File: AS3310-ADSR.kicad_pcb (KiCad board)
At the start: 2 copper layers, 58 parts, among them J1 TRIGGER_IN, J2 EURO_PWR_2x5, J3 ENVELOPE_OUT, J4 GATE_IN, Q1 BC558, Q2 BC548, SW2 SW_Push, U1 LM358, U2 AS3310, U3 LM358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

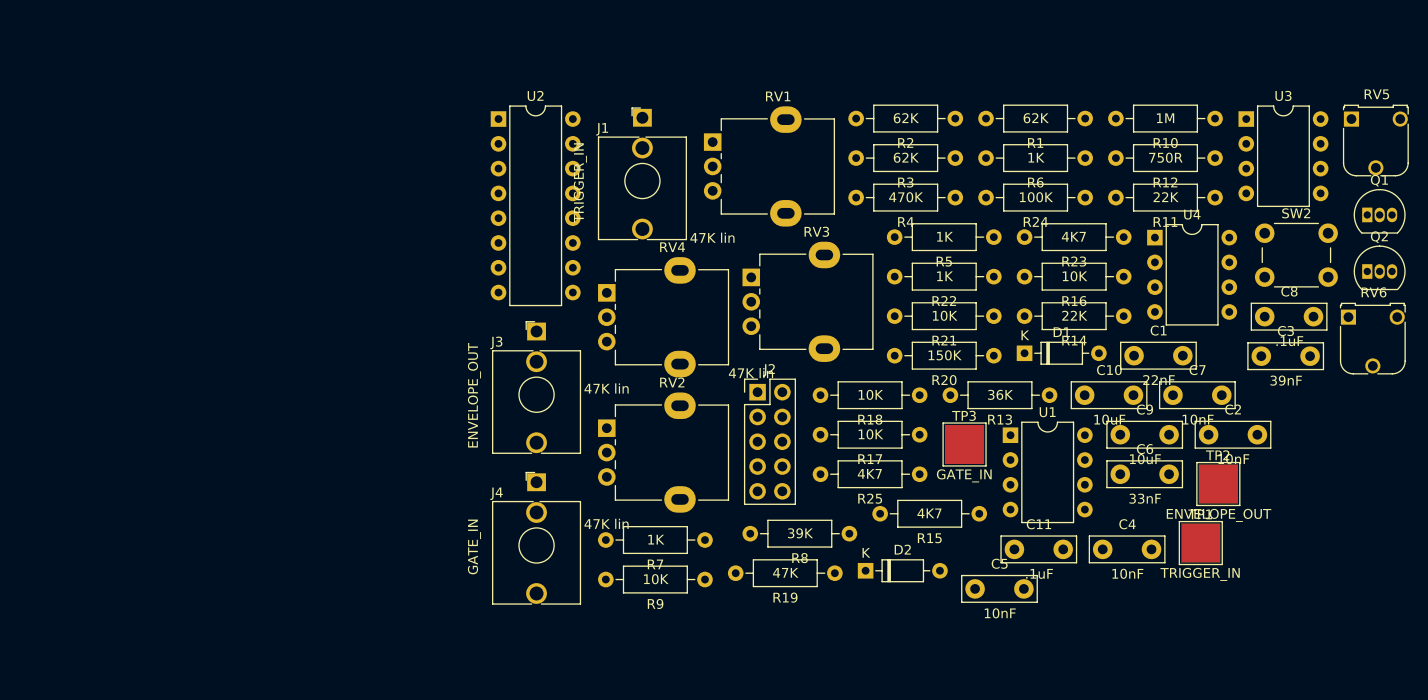
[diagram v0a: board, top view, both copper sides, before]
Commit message: Refactor DP3T switch.
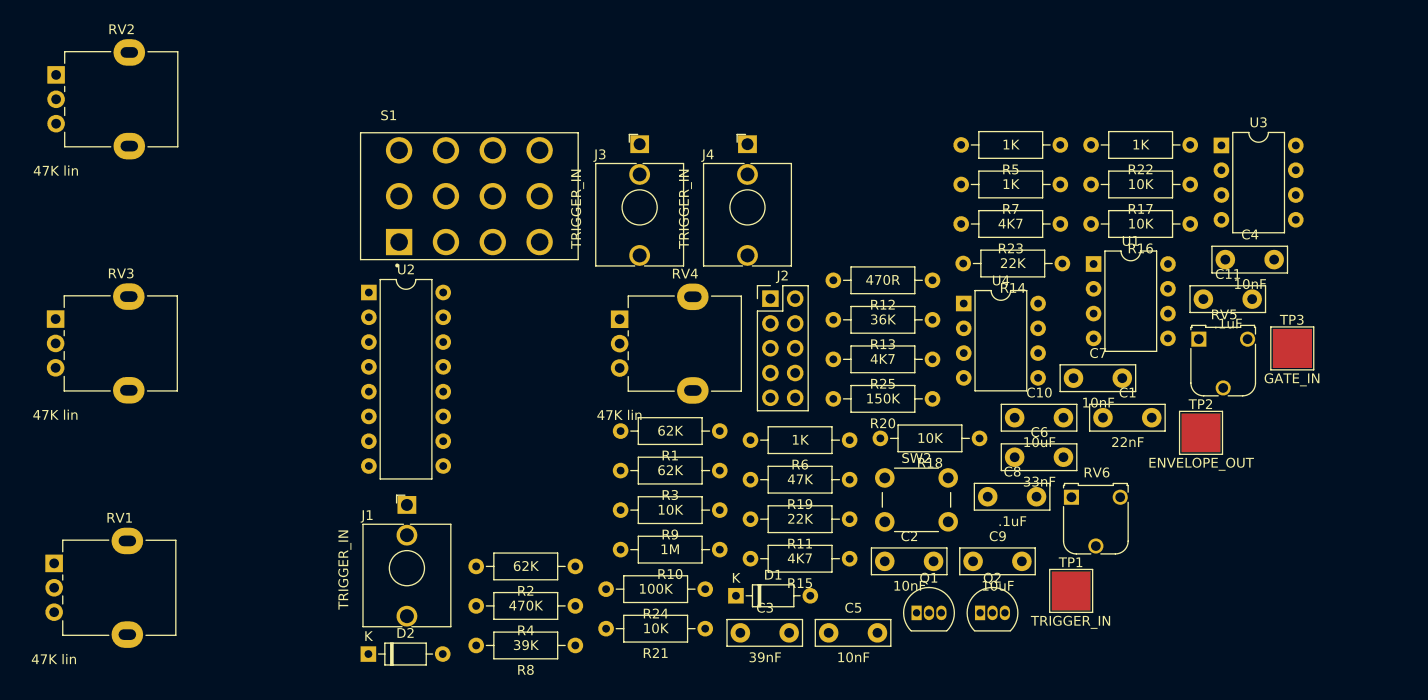
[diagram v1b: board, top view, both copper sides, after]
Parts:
- added S1: M2044SS1W03, Seattle_Synths:SW_M2044SS1W03, F.Cu at (102.1, 83.0)
- J3: value ENVELOPE_OUT -> TRIGGER_IN
- J4: value GATE_IN -> TRIGGER_IN
- R12: value 750R -> 470R
- moved RV1 80.1 mm to (59.6, 120.6)
- moved RV3 71.4 mm to (59.7, 95.5)
- moved R10 67.3 mm to (117.6, 119.2)
- moved RV2 67.1 mm to (59.8, 70.5)
- moved Q1 61.6 mm to (147.9, 125.7)
- moved C3 60.4 mm to (129.9, 127.7)
- moved R2 60.2 mm to (102.8, 120.9)
- moved R4 57.2 mm to (102.8, 124.9)
- moved R24 55.9 mm to (116.1, 123.2)
- moved Q2 52.9 mm to (154.4, 125.7)
- moved D2 51.7 mm to (91.8, 129.9)
- moved R7 51.5 mm to (152.5, 81.8)
- moved R11 49.9 mm to (130.9, 116.0)
- moved R1 49.3 mm to (117.6, 107.0)
- moved J1 46.4 mm to (95.7, 114.6)
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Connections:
- net Net-(C7-Pad1) renamed /OUT2
- net Net-(J4-PadT) renamed /IN1
- net Net-(Q2-Pad2) renamed /OUT3
- net Net-(R10-Pad1) renamed /OUT4
- C5 pad 2: (no net) -> /IN2
- C6 pad 1: (no net) -> /OUT1
